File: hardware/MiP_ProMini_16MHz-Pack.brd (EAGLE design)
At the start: 41.4 x 63.8 mm, 51 parts, among them Q1 16MHZ, U1 ATMEGA328, U2 MIC5205-5.0, U3 TS3USB221A, U4 MIC5205-3.3

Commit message: Version 3 - Route all power headers on top layer
Previously I had the upper right power rail in the user prototype area
routed on the bottom layer whereas the rest were routed on the bottom.
This commit makes them all the same and makes it easier for the user
to see which pads are connected to what just by looking at the traces
through the top soldermask.
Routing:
- net N$6: track 17.1 -> 11.2 mm, vias 1 -> 0
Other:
- board text added: "v3"
- board text removed: "v2"
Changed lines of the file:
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@@
 5V</text>
 <text x="35.306" y="-9.652" size="1.6764" layer="51" ratio="15">Adam Green</text>
-<text x="21.336" y="1.397" size="1.016" layer="22" font="vector" ratio="15" rot="MR0" align="center">v2</text>
+<text x="21.336" y="1.397" size="1.016" layer="22" font="vector" ratio="15" rot="MR0" align="center">v3</text>
 <text x="6.096" y="32.258" size="0.8128" layer="21" font="vector" ratio="15" align="center">GND</text>
 <text x="5.842" y="30.734" size="0.8128" layer="21" font="vector" ratio="15" align="center">RX</text>
@@
 <contactref element="JP8" pad="4"/>
 <contactref element="SJ4" pad="2"/>
-<wire x1="31.496" y1="46.228" x2="31.496" y2="43.688" width="0.3048" layer="16"/>
-<wire x1="31.496" y1="43.688" x2="31.496" y2="41.148" width="0.3048" layer="16"/>
-<wire x1="31.496" y1="41.148" x2="31.496" y2="38.608" width="0.3048" layer="16"/>
-<wire x1="31.496" y1="46.228" x2="31.496" y2="51.583790625" width="0.3048" layer="16"/>
-<wire x1="31.496" y1="51.583790625" x2="31.42160625" y2="51.76339375" width="0.3048" layer="16" curve="44.999502"/>
-<wire x1="31.42160625" y1="51.76339375" x2="30.734" y2="52.451" width="0.3048" layer="16"/>
-<via x="30.734" y="52.451" extent="1-16" drill="0.254" diameter="0.508"/>
-<wire x1="30.734" y1="52.451" x2="31.42160625" y2="51.76339375" width="0.3048" layer="1"/>
-<wire x1="31.42160625" y1="51.76339375" x2="31.496" y2="51.583790625" width="0.3048" layer="1" curve="-44.999295"/>
-<wire x1="31.496" y1="51.583790625" x2="31.496" y2="49.784" width="0.3048" layer="1"/>
+<wire x1="31.496" y1="49.784" x2="31.496" y2="46.228" width="0.3048" layer="1"/>
+<wire x1="31.496" y1="46.228" x2="31.496" y2="43.688" width="0.3048" layer="1"/>
+<wire x1="31.496" y1="43.688" x2="31.496" y2="41.148" width="0.3048" layer="1"/>
+<wire x1="31.496" y1="41.148" x2="31.496" y2="38.608" width="0.3048" layer="1"/>
 </signal>
 <signal name="VIN">

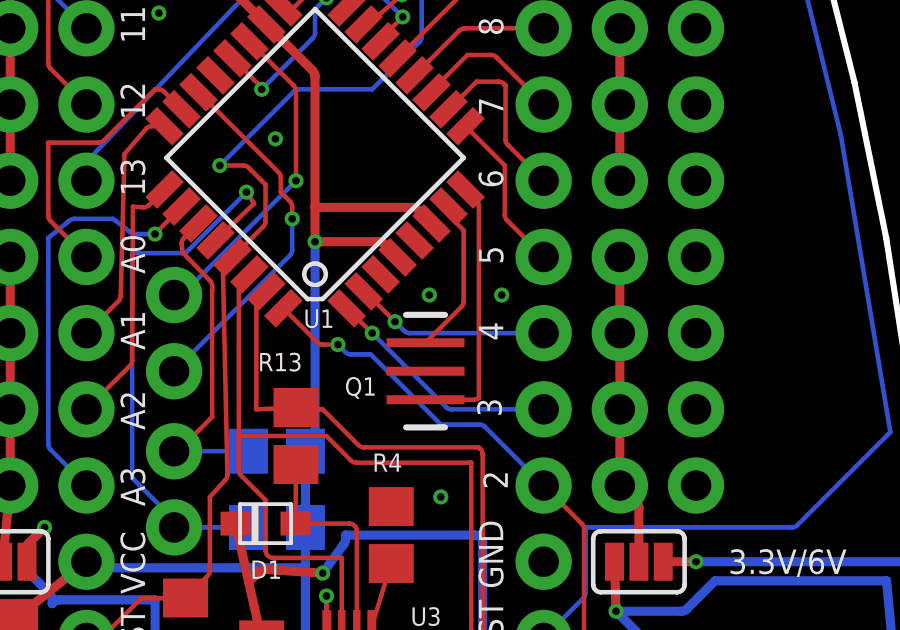
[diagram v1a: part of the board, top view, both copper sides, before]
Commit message: Added tRestrict to 16MHz resonator part
This keeps the ground plane and wires out of the tStop area that was
already defined for the resonator.
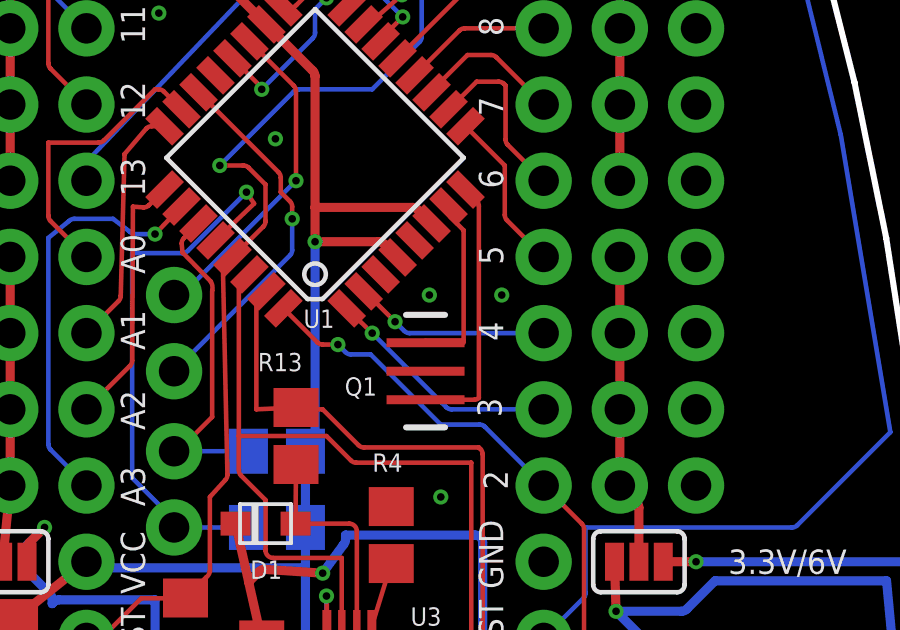
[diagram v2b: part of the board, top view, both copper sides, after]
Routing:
- net N$4: track 5.24 -> 6.07 mm
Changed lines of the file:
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@@
 <contactref element="U1" pad="8"/>
 <contactref element="Q1" pad="3"/>
-<wire x1="25.019" y1="31.308" x2="26.649734375" y2="31.308" width="0.1524" layer="1"/>
 <wire x1="26.649734375" y1="31.308" x2="26.797" y2="31.369" width="0.1524" layer="1" curve="45"/>
 <wire x1="26.797" y1="31.369" x2="26.797" y2="37.7635875" width="0.1524" layer="1"/>
 <wire x1="26.797" y1="37.7635875" x2="26.72260625" y2="37.943190625" width="0.1524" layer="1" curve="44.999502"/>
 <wire x1="26.72260625" y1="37.943190625" x2="26.351225" y2="38.314571875" width="0.1524" layer="1"/>
+<wire x1="26.649734375" y1="31.308" x2="25.019" y2="31.308" width="0.1524" layer="1"/>
 </signal>
 <signal name="N$4">
 <contactref element="U1" pad="7"/>
 <contactref element="Q1" pad="1"/>
-<wire x1="25.019" y1="33.208" x2="26.21460625" y2="34.40360625" width="0.1524" layer="1"/>
-<wire x1="26.21460625" y1="34.40360625" x2="26.289" y2="34.583209375" width="0.1524" layer="1" curve="44.999295"/>
-<wire x1="26.289" y1="34.583209375" x2="26.289" y2="36.957" width="0.1524" layer="1"/>
+<wire x1="26.289" y1="33.208" x2="26.289" y2="33.274" width="0.1524" layer="1"/>
+<wire x1="26.289" y1="33.274" x2="26.289" y2="36.957" width="0.1524" layer="1"/>
 <wire x1="26.289" y1="36.957" x2="25.85993125" y2="37.38606875" width="0.1524" layer="1"/>
 <wire x1="25.85993125" y1="37.38606875" x2="25.7855375" y2="37.565671875" width="0.1524" layer="1" curve="-44.999295"/>
 <wire x1="25.7855375" y1="37.565671875" x2="25.7855375" y2="37.748884375" width="0.1524" layer="1"/>
+<wire x1="25.019" y1="33.208" x2="25.019" y2="33.274" width="0.1524" layer="1"/>
+<wire x1="25.019" y1="33.274" x2="26.289" y2="33.274" width="0.1524" layer="1"/>
 </signal>
 <signal name="DTR">

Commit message: Add a 1k load across 3.3V supply
Without this load, the 3.3V supply was closer to 4.4V. The datasheet
for the regulator indicates that it doesn't have a minimum load to
maintain regulation but it also indicates that the output capacitance
can be closer to 0.5uF when the output current is only 1mA. If a
person was using the 3.3V supply for something else that was putting
a >= 1mA load on it then they could omit this resistor. Lowering the
output capacitance (which was copied from the original Sparkfun design)
might also correct the problem.
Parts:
- added R9: 1K, rcl:R0805
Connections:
- net 3.3V: now also R9.2
- net GND: now also R9.1
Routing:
- net 3.3V: track 96.4 -> 98.3 mm
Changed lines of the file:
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@@
 <attribute name="NAME" x="25.146" y="19.812" size="0.6096" layer="25" font="vector" rot="R270"/>
+</element>
+<element name="R9" library="rcl" package="R0805" value="1K" x="31.115" y="8.255" smashed="yes" rot="R90">
+<attribute name="NAME" x="29.845" y="7.62" size="0.6096" layer="25" font="vector" rot="R90"/>
 </element>
 </elements>
@@
 <via x="16.129" y="16.002" extent="1-16" drill="0.254" diameter="0.508"/>
 <via x="25.527" y="28.067" extent="1-16" drill="0.254" diameter="0.508"/>
+<contactref element="R9" pad="1"/>
 </signal>
 <signal name="AREF">
@@
 </signal>
 <signal name="3.3V">
-<contactref element="U4" pad="5"/>
-<contactref element="C6" pad="A"/>
-<contactref element="C5" pad="1"/>
 <contactref element="C4" pad="2"/>
 <contactref element="U3" pad="10"/>
 <contactref element="D1" pad="C"/>
-<wire x1="23.0171" y1="10.729" x2="25.654" y2="12.322" width="0.3048" layer="1"/>
-<wire x1="25.654" y1="12.322" x2="28.956" y2="11.237" width="0.3048" layer="1"/>
 <contactref element="SJ1" pad="3"/>
 <contactref element="SJ2" pad="3"/>
@@
 <via x="34.036" y="13.208" extent="1-16" drill="0.254" diameter="0.508"/>
 <wire x1="34.036" y1="13.208" x2="34.036" y2="11.491" width="0.3048" layer="1"/>
-<wire x1="34.036" y1="11.491" x2="33.782" y2="11.237" width="0.3048" layer="1" curve="-90"/>
-<wire x1="33.782" y1="11.237" x2="28.956" y2="11.237" width="0.3048" layer="1"/>
 <wire x1="21.379" y1="22.86" x2="20.105209375" y2="22.86" width="0.3048" layer="1"/>
 <wire x1="20.105209375" y1="22.86" x2="19.92560625" y2="22.93439375" width="0.3048" layer="1" curve="-44.999502"/>
@@
 <wire x1="19.650159375" y1="25.654" x2="19.47055625" y2="25.57960625" width="0.3048" layer="1" curve="44.999502"/>
 <wire x1="19.47055625" y1="25.57960625" x2="19.1232375" y2="25.2322875" width="0.3048" layer="1"/>
+<contactref element="U4" pad="5"/>
+<contactref element="C6" pad="A"/>
+<contactref element="C5" pad="1"/>
+<contactref element="R9" pad="2"/>
+<wire x1="23.0171" y1="10.729" x2="25.654" y2="12.322" width="0.3048" layer="1"/>
+<wire x1="25.654" y1="12.322" x2="28.956" y2="11.237" width="0.3048" layer="1"/>
+<wire x1="28.956" y1="11.237" x2="30.292" y2="11.237" width="0.3048" layer="1"/>
+<wire x1="30.292" y1="11.237" x2="31.115" y2="10.414" width="0.3048" layer="1"/>
+<wire x1="31.115" y1="10.414" x2="31.115" y2="9.205" width="0.3048" layer="1"/>
+<wire x1="34.036" y1="11.491" x2="32.959" y2="10.414" width="0.3048" layer="1"/>
+<wire x1="32.959" y1="10.414" x2="31.115" y2="10.414" width="0.3048" layer="1"/>
 </signal>
 <signal name="N$15">
